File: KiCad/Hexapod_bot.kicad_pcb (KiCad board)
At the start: 4 copper layers, 68 x 80 mm, 126 parts, among them J1 Ras Pi 4 Interface, J10 Conn_01x03, J11 Conn_01x03, J12 Conn_01x03, J13 Conn_01x03, J14 Conn_01x03, J15 Conn_01x03, J16 Conn_01x03, J17 Conn_01x03, J18 Conn_01x03, J19 Conn_01x03, J2 Leg Switches, J20 Conn_01x03, J21 Conn_01x03, J22 Conn_01x03, J23 Conn_01x03, J24 Conn_01x03, J25 Conn_01x03, J3 Terminal Block, J4 Conn_01x03, J5 Conn_01x03, J6 Conn_01x03, J7 Conn_01x03, J8 Conn_01x03, J9 Conn_01x03, Q1 BSS138, Q2 BSS138, Q3 BSS138, Q4 BSS138, U1 LM25085MM/NOPB, U2 TPS563231DRLR, U3 CSD25402Q3A, U4 LM78L05_SO8, U5 LM393, U6 PCA9685PW, U7 PCA9685PW, U8 LSM6DSO32TR

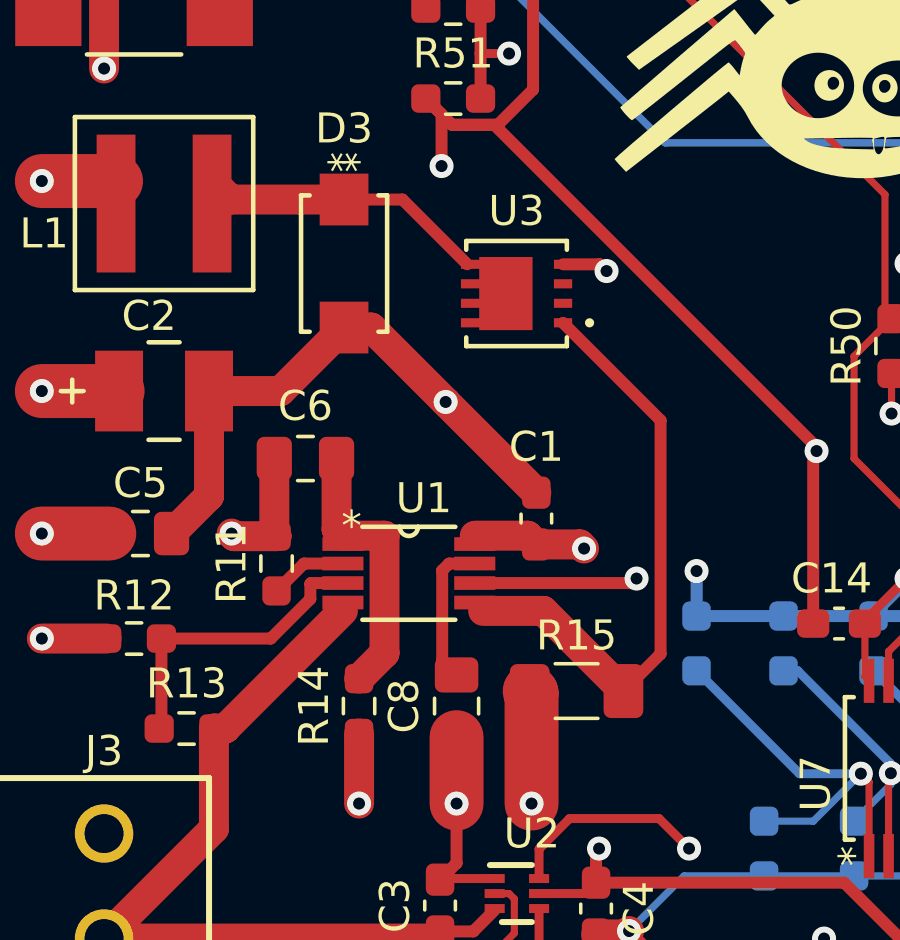
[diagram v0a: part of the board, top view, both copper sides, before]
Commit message: Changed 6V power line schematic
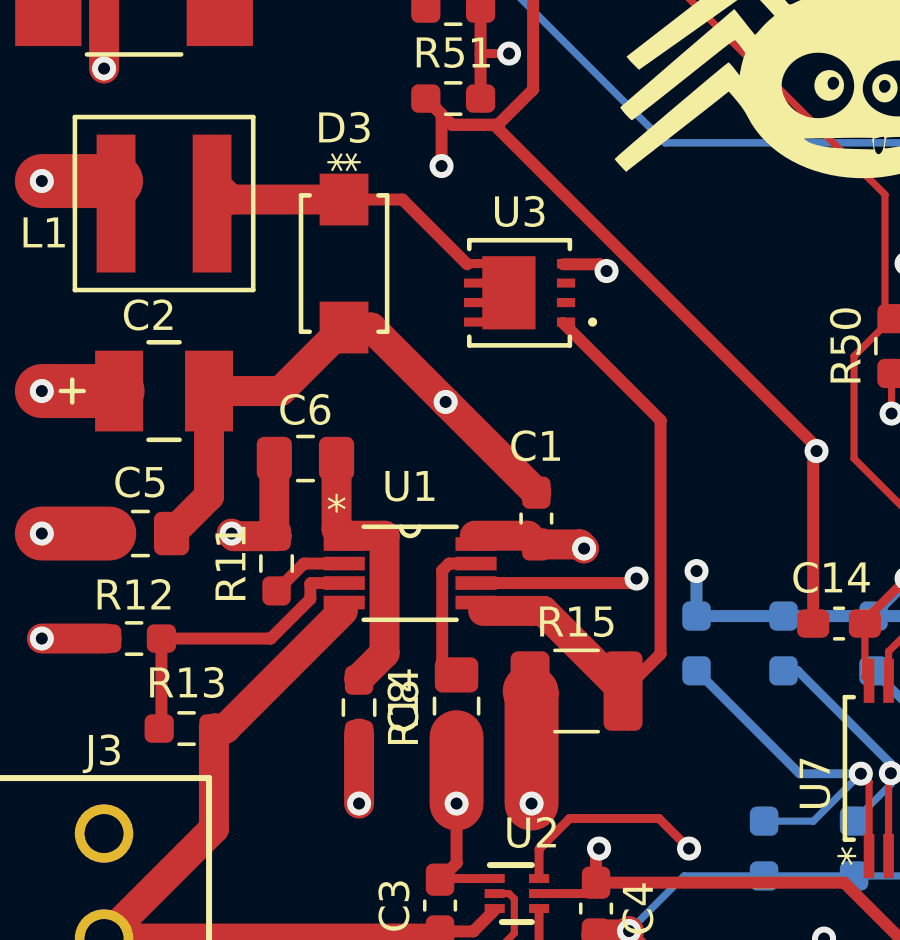
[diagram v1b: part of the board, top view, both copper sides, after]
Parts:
- C10, C15, C16, C4, C7: value 100nF -> 0.1uF
- C11, C12: value 0.1 -> 0.1F
- R15: footprint Capacitor_SMD:C_1206_3216Metric_Pad1.33x1.80mm_HandSolder -> Resistor_SMD:R_1210_3225Metric_Pad1.30x2.65mm_HandSolder
- U1: footprint Spiderbot:MUA08A -> myLib:MUA08A
- U3: footprint Spiderbot:CSD25402Q3A -> myLib:CSD25402Q3A
- moved U3 0.10 mm to (12.9, 21.5)
- turned R14 to 90 degrees
- turned C6 to 0 degrees
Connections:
- C6 pad 1: Net-(U1-ADJ) -> 7.4V_batt
- C6 pad 2: 7.4V_batt -> Net-(U1-ADJ)
- R14 pad 1: Net-(U1-ADJ) -> 7.4V_batt
- R14 pad 2: 7.4V_batt -> Net-(U1-ADJ)
- U3 pad 2: unconnected-(U3-D-Pad2) -> Net-(U1-ISEN)
- U3 pad 3: unconnected-(U3-D-Pad3) -> Net-(U1-ISEN)
- U3 pad 6: unconnected-(U3-S-Pad6) -> Net-(D3-K)
- U3 pad 7: unconnected-(U3-S-Pad7) -> Net-(D3-K)
- U3 pad 8: unconnected-(U3-S-Pad8) -> Net-(D3-K)
- U3 pad 9: unconnected-(U3-S-Pad9) -> Net-(D3-K)
